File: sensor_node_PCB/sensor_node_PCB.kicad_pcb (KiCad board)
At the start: 2 copper layers, 102.6 x 47.7 mm, 51 parts, among them J1 USB_B_Mini, J2 INPUT CONNECTOR, J3 OUTPUT_CONNECTOR, P1 BREAKOUTS, Q1 FDN340P, Q2 BSS138, Q3 BSS138, SW1 RESET_SWITCH, U1 LMV358IDGKR, U2 LD1117S50TR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

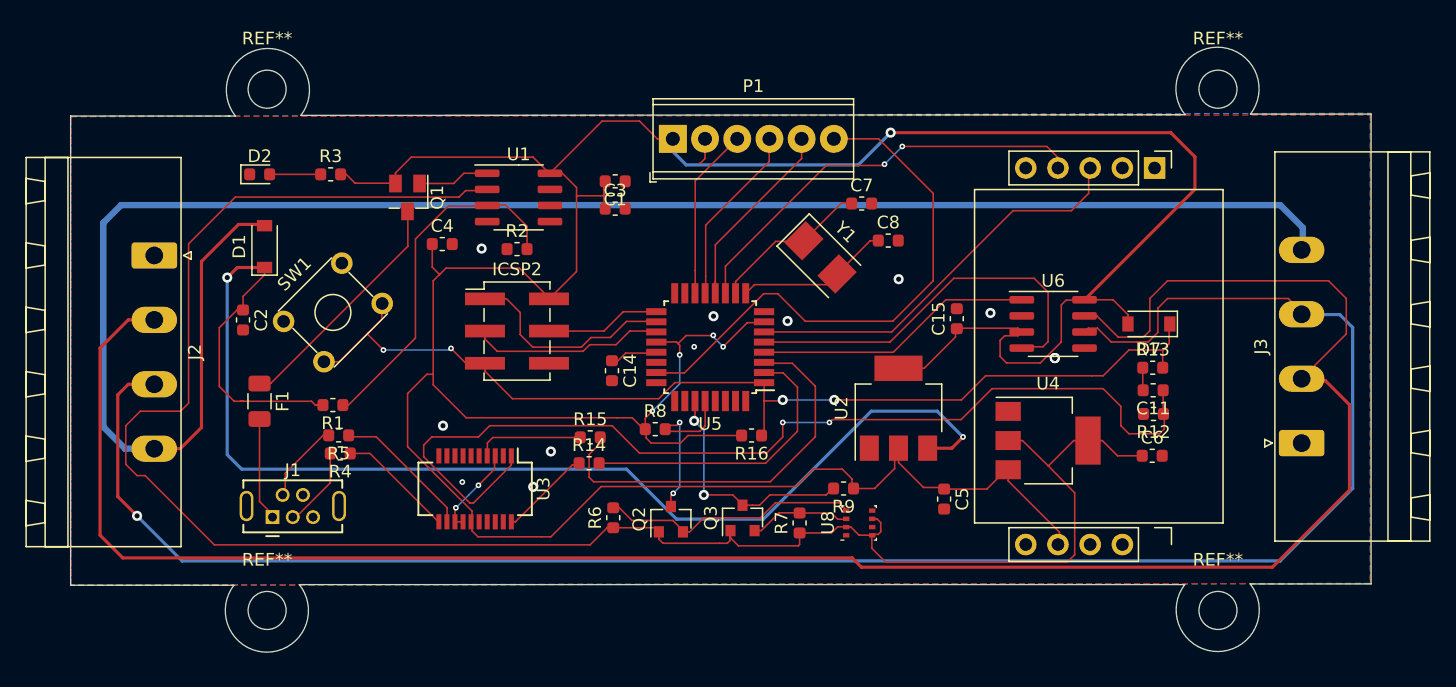
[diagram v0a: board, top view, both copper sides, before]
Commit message: fixed senseair s8 pin mixup - added lots of silk text
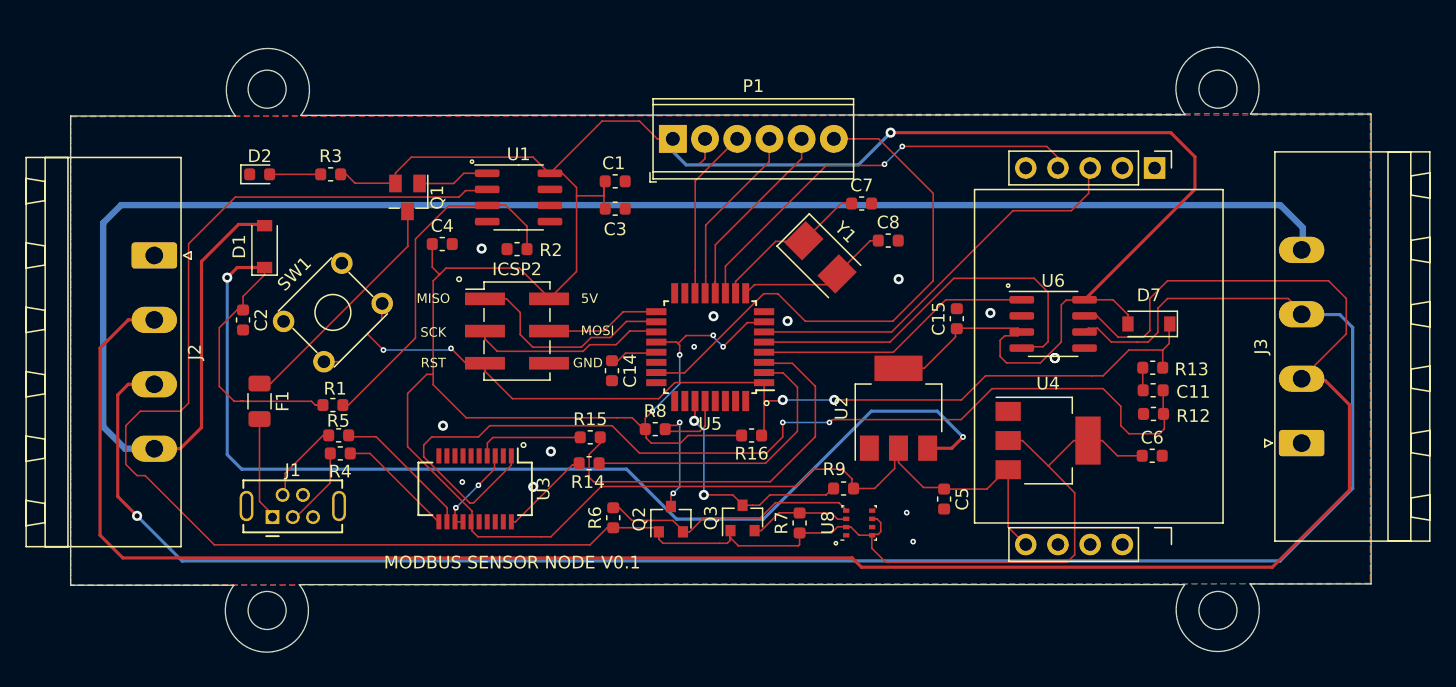
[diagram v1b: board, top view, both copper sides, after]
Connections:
- U7 pad 1: GND -> 5V_LDO
- U7 pad 2: 5V_LDO -> GND
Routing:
- net 5V_LDO: track 276.4 -> 275.3 mm
- net GND: vias 12 -> 14
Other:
- board text added: "5V"
- board text added: "GND"
- board text added: "MISO"
- board text added: "MODBUS SENSOR NODE V0.1"
- board text added: "MOSI"
- board text added: "RST"
- board text added: "SCK"
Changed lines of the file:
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@@
   (general
     (thickness 1.6)
-    (drawings 16)
-    (tracks 516)
+    (drawings 28)
+    (tracks 517)
     (zones 0)
     (modules 51)
@@
     (35 F.Paste user hide)
     (36 B.SilkS user hide)
-    (37 F.SilkS user hide)
+    (37 F.SilkS user)
     (38 B.Mask user hide)
     (39 F.Mask user hide)
@@
   )
   (setup
-    (last_trace_width 0.25)
+    (last_trace_width 0.127)
     (user_trace_width 0.127)
     (user_trace_width 0.5)
@@
     (tags "mounting hole 3mm no annular")
     (attr virtual)
-    (fp_text reference REF** (at 0 -4) (layer F.SilkS)
+    (fp_text reference REF** (at 0 -4) (layer F.SilkS) hide
       (effects (font (size 1 1) (thickness 0.15)))
     )
@@
     (tags "mounting hole 3mm no annular")
     (attr virtual)
-    (fp_text reference REF** (at 0 -4) (layer F.SilkS)
+    (fp_text reference REF** (at 0 -4) (layer F.SilkS) hide
       (effects (font (size 1 1) (thickness 0.15)))
     )
@@
     (tags "mounting hole 3mm no annular")
     (attr virtual)
-    (fp_text reference REF** (at 0 -4) (layer F.SilkS)
+    (fp_text reference REF** (at 0 -4) (layer F.SilkS) hide
       (effects (font (size 1 1) (thickness 0.15)))
     )
@@
     (tags "mounting hole 3mm no annular")
     (attr virtual)
-    (fp_text reference REF** (at 0 -4) (layer F.SilkS)
+    (fp_text reference REF** (at 0 -4) (layer F.SilkS) hide
       (effects (font (size 1 1) (thickness 0.15)))
     )
@@
     (tags capacitor)
     (attr smd)
-    (fp_text reference C1 (at 0 -1.43) (layer F.SilkS)
+    (fp_text reference C1 (at 0.12 1.425) (layer F.SilkS)
       (effects (font (size 1 1) (thickness 0.15)))
     )
@@
     (tags capacitor)
     (attr smd)
-    (fp_text reference C3 (at 0 -1.43) (layer F.SilkS)
+    (fp_text reference C3 (at 0 1.623) (layer F.SilkS)
       (effects (font (size 1 1) (thickness 0.15)))
     )
@@
     (tags capacitor)
     (attr smd)
-    (fp_text reference C11 (at 0 -1.43) (layer F.SilkS)
+    (fp_text reference C11 (at -3.1675 -0.127) (layer F.SilkS)
       (effects (font (size 1 1) (thickness 0.15)))
     )
@@
     (tags SOD-123)
     (attr smd)
-    (fp_text reference D7 (at 0 -2) (layer F.SilkS)
+    (fp_text reference D7 (at 0 2.26) (layer F.SilkS)
       (effects (font (size 1 1) (thickness 0.15)))
     )
@@
     (tags resistor)
     (attr smd)
-    (fp_text reference R1 (at 0 -1.43) (layer F.SilkS)
+    (fp_text reference R1 (at -0.1765 1.294) (layer F.SilkS)
       (effects (font (size 1 1) (thickness 0.15)))
     )
@@
     (tags resistor)
     (attr smd)
-    (fp_text reference R2 (at 0 -1.43) (layer F.SilkS)
+    (fp_text reference R2 (at 2.6695 0.084) (layer F.SilkS)
       (effects (font (size 1 1) (thickness 0.15)))
     )
@@
     (tags resistor)
     (attr smd)
-    (fp_text reference R5 (at 0 -1.43) (layer F.SilkS)
+    (fp_text reference R5 (at 0.0255 1.143) (layer F.SilkS)
       (effects (font (size 1 1) (thickness 0.15)))
     )
@@
     (tags resistor)
     (attr smd)
-    (fp_text reference R9 (at 0 -1.43) (layer F.SilkS)
+    (fp_text reference R9 (at 0.7365 1.524) (layer F.SilkS)
       (effects (font (size 1 1) (thickness 0.15)))
     )
@@
     (tags resistor)
     (attr smd)
-    (fp_text reference R12 (at 0 -1.43) (layer F.SilkS)
+    (fp_text reference R12 (at -3.1425 -0.165) (layer F.SilkS)
       (effects (font (size 1 1) (thickness 0.15)))
     )
@@
     (tags resistor)
     (attr smd)
-    (fp_text reference R13 (at 0 -1.43) (layer F.SilkS)
+    (fp_text reference R13 (at 3.0735 0.127) (layer F.SilkS)
       (effects (font (size 1 1) (thickness 0.15)))
     )
@@
     (tags resistor)
     (attr smd)
-    (fp_text reference R14 (at 0 -1.43) (layer F.SilkS)
+    (fp_text reference R14 (at -0.0945 1.4833) (layer F.SilkS)
       (effects (font (size 1 1) (thickness 0.15)))
     )
@@
       (net 59 "Net-(U7-Pad4)"))
     (pad 1 thru_hole oval (at -12.7 2.84 270) (size 1.7 1.7) (drill 1) (layers *.Cu *.Mask)
-      (net 2 GND))
+      (net 1 5V_LDO))
     (pad 3 thru_hole oval (at -12.7 7.92 270) (size 1.7 1.7) (drill 1) (layers *.Cu *.Mask)
       (net 58 "Net-(U7-Pad3)"))
     (pad 2 thru_hole oval (at -12.7 5.38 270) (size 1.7 1.7) (drill 1) (layers *.Cu *.Mask)
-      (net 1 5V_LDO))
+      (net 2 GND))
   )
   (module Connector_USB:USB_Mini-B_Tensility_54-00023_Vertical (layer F.Cu)
@@
     )
   )
+  (gr_text "MODBUS SENSOR NODE V0.1" (at 132.334 125.222) (layer F.SilkS)
+    (effects (font (size 1 1) (thickness 0.15)))
+  )
+  (gr_circle (center 152.4 112.649) (end 152.527 112.776) (layer F.SilkS) (width 0.12))
+  (gr_circle (center 133.223 115.951) (end 133.35 116.078) (layer F.SilkS) (width 0.12))
+  (gr_circle (center 157.861 123.698) (end 157.861 123.825) (layer F.SilkS) (width 0.12))
+  (gr_circle (center 171.45 103.378) (end 171.45 103.505) (layer F.SilkS) (width 0.12))
+  (gr_circle (center 129.159 93.599) (end 129.159 93.726) (layer F.SilkS) (width 0.12))
+  (gr_text GND (at 138.303 109.474) (layer F.SilkS)
+    (effects (font (size 0.75 0.75) (thickness 0.15)))
+  )
+  (gr_text MOSI (at 139.065 106.934) (layer F.SilkS)
+    (effects (font (size 0.75 0.75) (thickness 0.15)))
+  )
+  (gr_text 5V (at 138.43 104.394) (layer F.SilkS)
+    (effects (font (size 0.75 0.75) (thickness 0.15)))
+  )
+  (gr_text RST (at 126.111 109.474) (layer F.SilkS)
+    (effects (font (size 0.75 0.75) (thickness 0.15)))
+  )
+  (gr_text SCK (at 126.111 107.061) (layer F.SilkS)
+    (effects (font (size 0.75 0.75) (thickness 0.15)))
+  )
+  (gr_text MISO (at 126.111 104.394) (layer F.SilkS)
+    (effects (font (size 0.75 0.75) (thickness 0.15)))
+  )
+  (gr_circle (center 128.143 102.87) (end 128.27 102.997) (layer F.SilkS) (width 0.12))
   (dimension 102.746846 (width 0.15) (layer Dwgs.User)
     (gr_text "102.747 mm" (at 148.930159 76.239143 359.5042516) (layer Dwgs.User)
@@
     (arrow2a (pts (xy 88.776684 89.97185) (xy 88.194138 91.100362)))
     (arrow2b (pts (xy 88.776684 89.97185) (xy 89.366972 91.096332)))
-  )
-  (dimension 1.909229 (width 0.12) (layer F.SilkS)
-    (gr_text "1.909 mm" (at 101.907198 63.154968 3.814074834) (layer F.SilkS)
-      (effects (font (size 1 1) (thickness 0.15)))
-    )
-    (feature1 (pts (xy 104.648 89.916) (xy 102.905169 63.773533)))
-    (feature2 (pts (xy 102.743 90.043) (xy 101.000169 63.900533)))
-    (crossbar (pts (xy 101.039177 64.485655) (xy 102.944177 64.358655)))
-    (arrow1a (pts (xy 102.944177 64.358655) (xy 101.859176 65.018711)))
-    (arrow1b (pts (xy 102.944177 64.358655) (xy 101.78116 63.848467)))
-    (arrow2a (pts (xy 101.039177 64.485655) (xy 102.202194 64.995843)))
-    (arrow2b (pts (xy 101.039177 64.485655) (xy 102.124178 63.825599)))
   )
   (gr_line (start 115.541438 126.960848) (end 185.38 126.96) (layer Edge.Cuts) (width 0.05))
@@
   (segment (start 166.4 119.425) (end 169.775 119.425) (width 0.127) (layer F.Cu) (net 1))
   (segment (start 169.775 119.425) (end 171.3 117.9) (width 0.127) (layer F.Cu) (net 1))
-  (segment (start 171.45 118.777) (end 175.5 122.827) (width 0.127) (layer F.Cu) (net 1))
-  (segment (start 171.45 117.9) (end 171.45 118.777) (width 0.127) (layer F.Cu) (net 1))
-  (segment (start 175.5 122.827) (end 175.5 123.8) (width 0.127) (layer F.Cu) (net 1))
   (segment (start 172.225 106.735) (end 167.435 106.735) (width 0.127) (layer F.Cu) (net 1))
   (segment (start 172.525 107.035) (end 172.225 106.735) (width 0.127) (layer F.Cu) (net 1))
@@
   (segment (start 126.6 102.5) (end 126.608 102.5) (width 0.127) (layer F.Cu) (net 1))
   (segment (start 126.608 102.5) (end 127.108 102) (width 0.127) (layer F.Cu) (net 1))
+  (segment (start 171.45 117.9) (end 171.45 122.428) (width 0.127) (layer F.Cu) (net 1))
+  (segment (start 171.45 122.428) (end 172.847 123.825) (width 0.127) (layer F.Cu) (net 1))
   (via (at 175.133 109.093) (size 0.8) (drill 0.4) (layers F.Cu B.Cu) (net 2))
   (via (at 175.133 109.093) (size 0.8) (drill 0.4) (layers F.Cu B.Cu) (net 2))
@@
   (via (at 146.685 108.204) (size 0.45) (drill 0.2) (layers F.Cu B.Cu) (net 2))
   (via (at 128.397 118.872) (size 0.45) (drill 0.2) (layers F.Cu B.Cu) (net 2))
+  (via (at 163.449 121.285) (size 0.45) (drill 0.2) (layers F.Cu B.Cu) (net 2))
+  (via (at 163.957 123.571) (size 0.45) (drill 0.2) (layers F.Cu B.Cu) (net 2))
   (segment (start 116.9625 112.8) (end 117.4 112.8) (width 0.127) (layer F.Cu) (net 3))
   (segment (start 116.8 112.8) (end 116.9625 112.8) (width 0.127) (layer F.Cu) (net 3))

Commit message: changed board outline to rectangle
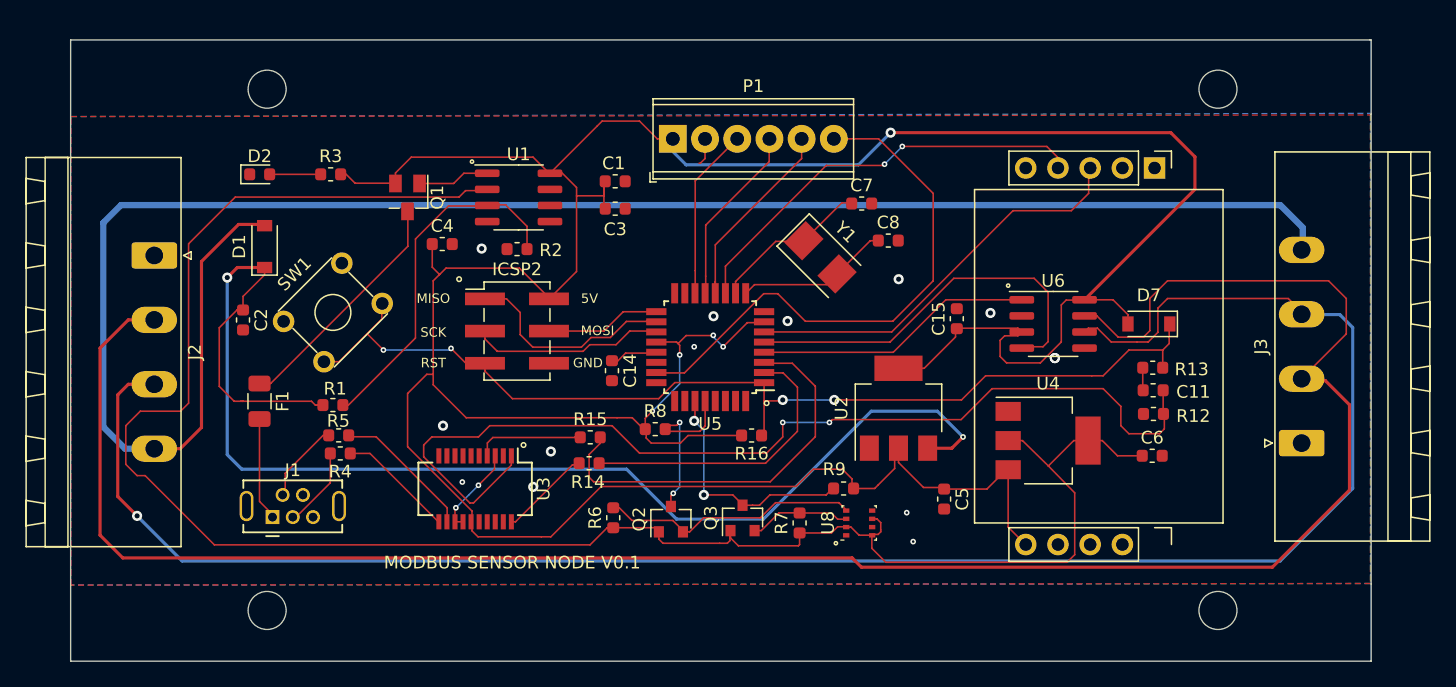
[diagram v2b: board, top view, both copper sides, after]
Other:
- board size 102.6 x 47.7 mm -> 102.6 x 49 mm
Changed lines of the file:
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@@
   (general
     (thickness 1.6)
-    (drawings 28)
+    (drawings 24)
     (tracks 517)
     (zones 0)
@@
   )
   (setup
-    (last_trace_width 0.127)
+    (last_trace_width 0.25)
     (user_trace_width 0.127)
     (user_trace_width 0.5)
@@
     )
   )
+  (gr_line (start 200.08 126.91) (end 200.08 133) (layer Edge.Cuts) (width 0.05))
+  (gr_line (start 97.5 133) (end 200.08 133) (layer Edge.Cuts) (width 0.05))
+  (gr_line (start 97.5 127.01) (end 97.5 133) (layer Edge.Cuts) (width 0.05))
+  (gr_line (start 200 84) (end 200.08 84) (layer Edge.Cuts) (width 0.05))
+  (gr_line (start 200.08 89.85) (end 200.08 84) (layer Edge.Cuts) (width 0.05))
+  (gr_line (start 97.5 84) (end 200 84) (layer Edge.Cuts) (width 0.05))
+  (gr_line (start 97.5 90) (end 97.5 84) (layer Edge.Cuts) (width 0.05))
   (gr_text "MODBUS SENSOR NODE V0.1" (at 132.334 125.222) (layer F.SilkS)
     (effects (font (size 1 1) (thickness 0.15)))
@@
     (arrow2b (pts (xy 88.776684 89.97185) (xy 89.366972 91.096332)))
   )
-  (gr_line (start 115.541438 126.960848) (end 185.38 126.96) (layer Edge.Cuts) (width 0.05))
-  (gr_line (start 97.5 127.01) (end 110.38 127.01) (layer Edge.Cuts) (width 0.05))
   (gr_line (start 97.5 90) (end 97.5 127.01) (layer Edge.Cuts) (width 0.05))
-  (gr_arc (start 112.979999 129.009999) (end 110.38 127.01) (angle -256.2284003) (layer Edge.Cuts) (width 0.05))
-  (gr_line (start 200.08 126.91) (end 190.541438 126.910848) (layer Edge.Cuts) (width 0.05))
   (gr_line (start 200.08 89.85) (end 200.08 126.91) (layer Edge.Cuts) (width 0.05))
-  (gr_arc (start 187.979999 128.959999) (end 185.38 126.96) (angle -256.2284003) (layer Edge.Cuts) (width 0.05))
-  (gr_line (start 190.561438 89.850848) (end 200.08 89.85) (layer Edge.Cuts) (width 0.05))
-  (gr_line (start 115.661438 89.950848) (end 185.4 89.9) (layer Edge.Cuts) (width 0.05))
-  (gr_arc (start 187.961439 87.850849) (end 190.561438 89.850848) (angle -256.2284003) (layer Edge.Cuts) (width 0.05))
-  (gr_line (start 110 90) (end 110.5 90) (layer Edge.Cuts) (width 0.05))
-  (gr_arc (start 113.061439 87.950849) (end 115.661438 89.950848) (angle -256.2284003) (layer Edge.Cuts) (width 0.05))
-  (gr_line (start 110 90) (end 97.5 90) (layer Edge.Cuts) (width 0.05))
   (segment (start 136.285 94.516) (end 137.407 95.638) (width 0.127) (layer F.Cu) (net 1))
   (segment (start 135.31 94.516) (end 136.285 94.516) (width 0.127) (layer F.Cu) (net 1))
@@
   (segment (start 157.955648 102.453548) (end 160.571896 99.8373) (width 0.127) (layer F.Cu) (net 6))
   (segment (start 160.571896 99.8373) (end 161.1814 99.8373) (width 0.127) (layer F.Cu) (net 6))
-  (segment (start 183.675 113.475) (end 183.8 113.6) (width 0.127) (layer F.Cu) (net 38))
-  (segment (start 183.675 111.633) (end 183.675 113.378) (width 0.127) (layer F.Cu) (net 38))
   (segment (start 182.067 109.855) (end 182.067 111.684) (width 0.127) (layer F.Cu) (net 7))
   (segment (start 182.067 111.684) (end 181.991 111.76) (width 0.127) (layer F.Cu) (net 7))
@@
   (segment (start 156.2411 111.3181) (end 154.425 109.502) (width 0.127) (layer F.Cu) (net 37))
   (segment (start 154.425 109.502) (end 152.2787 109.502) (width 0.127) (layer F.Cu) (net 37))
+  (segment (start 183.675 113.475) (end 183.8 113.6) (width 0.127) (layer F.Cu) (net 38))
+  (segment (start 183.675 111.633) (end 183.675 113.378) (width 0.127) (layer F.Cu) (net 38))
   (segment (start 132.2635 117.535) (end 129.2755 120.523) (width 0.127) (layer F.Cu) (net 38))
   (segment (start 132.2635 116.808) (end 132.2635 117.535) (width 0.127) (layer F.Cu) (net 38))
